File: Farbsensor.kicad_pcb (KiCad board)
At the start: 2 copper layers, 17.8 x 10.5 mm, 9 parts, among them J1 Conn_02x03_Odd_Even, Q1 BCW32

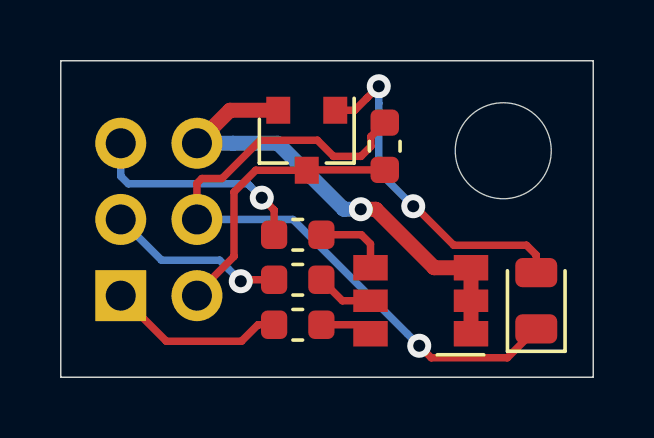
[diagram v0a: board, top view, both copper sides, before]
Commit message: changed pin header assignment, moved resistor
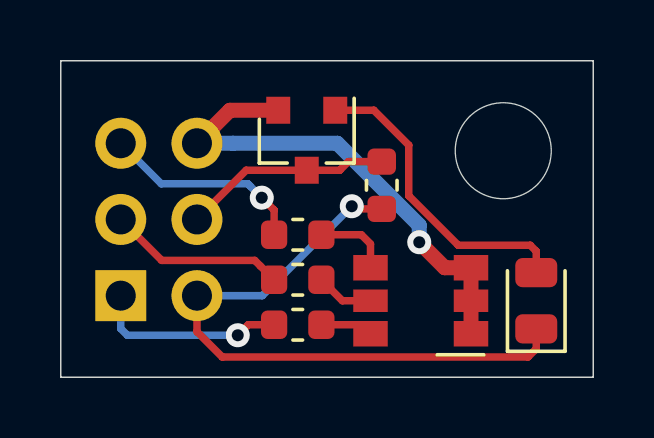
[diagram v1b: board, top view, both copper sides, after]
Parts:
- moved R1 1.30 mm to (107.7, 90.9), turned to 90 degrees
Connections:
- J1 pad 2: /SEN -> +5V
- J1 pad 4: +5V -> /SEN
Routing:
- net /SEN: track 9.30 -> 6.98 mm
- net +5V: track 22.6 -> 21.1 mm
- net Net-(D1-Pad2): track 11.6 -> 10.3 mm, vias 2 -> 0
- net /LED_B: track 7.50 -> 6.86 mm
- net /LED_R: track 5.97 -> 6.45 mm, vias 0 -> 1
- net /LED_G: track 5.99 -> 5.95 mm, vias 1 -> 0

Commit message: Layout überarbeitet, Beschriftungsfehler behoben
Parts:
- moved R2 3.00 mm to (104.9, 95.5)
- moved R4 3.00 mm to (104.9, 92.5)
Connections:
- net Net-(D2-Pad4) renamed /R
- net Net-(D2-Pad5) renamed /G
- net Net-(D2-Pad6) renamed /B
- J1 pad 1: /LED_R -> /LED_B
- J1 pad 5: /LED_B -> /LED_R
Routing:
- net /R: track 1.76 -> 2.56 mm
- net /B: track 2.56 -> 1.76 mm
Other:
- board text added: "Carlo v1.1 Brokering"
- board text removed: "v1.0 Carlo Brokering"

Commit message: Beschriftung geändert
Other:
- board text added: "Farbsensor v1.1"
- board text removed: "Carlo v1.1 Brokering"
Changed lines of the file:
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@@
   (gr_line (start 113.75 94.75) (end 110.7 94.75) (layer B.SilkS) (width 1))
   (target plus (at 104.9 95.55) (size 5) (width 0.05) (layer Edge.Cuts))
-  (gr_text "Carlo v1.1 \nBrokering" (at 108.05 88.15 90) (layer B.SilkS)
-    (effects (font (size 1 1) (thickness 0.2)) (justify left mirror))
+  (gr_text "Farbsensor\nv1.1" (at 108.05 92.05 90) (layer B.SilkS)
+    (effects (font (size 1 1) (thickness 0.2)) (justify mirror))
   )
   (gr_text SEN (at 105.35 92.04 90) (layer B.SilkS)
@@
   (segment (start 102.742081 89.5) (end 101.54 89.5) (width 0.5) (layer B.Cu) (net 3))
   (segment (start 108.95 92.8) (end 108.95 92.234315) (width 0.5) (layer B.Cu) (net 3))
-  (segment (start 107.025 95.55) (end 107.325 95.85) (width 0.25) (layer F.Cu) (net 10))
-  (segment (start 105.6875 95.55) (end 107.025 95.55) (width 0.25) (layer F.Cu) (net 10))
-  (segment (start 106.3875 94.75) (end 107.325 94.75) (width 0.25) (layer F.Cu) (net 9))
-  (segment (start 105.6875 94.05) (end 106.3875 94.75) (width 0.25) (layer F.Cu) (net 9))
-  (segment (start 107.325 92.85625) (end 107.325 93.65) (width 0.25) (layer F.Cu) (net 8))
-  (segment (start 107.01875 92.55) (end 107.325 92.85625) (width 0.25) (layer F.Cu) (net 8))
-  (segment (start 105.6875 92.55) (end 107.01875 92.55) (width 0.25) (layer F.Cu) (net 8))
+  (via (at 102.9 95.9) (size 0.8) (drill 0.4) (layers F.Cu B.Cu) (net 4))
+  (segment (start 104.1125 95.55) (end 103.25 95.55) (width 0.25) (layer F.Cu) (net 4))
+  (segment (start 103.25 95.55) (end 102.9 95.9) (width 0.25) (layer F.Cu) (net 4))
+  (segment (start 99.22 95.9) (end 99 95.68) (width 0.25) (layer B.Cu) (net 4))
+  (segment (start 99 95.68) (end 99 94.58) (width 0.25) (layer B.Cu) (net 4))
+  (segment (start 102.9 95.9) (end 99.22 95.9) (width 0.25) (layer B.Cu) (net 4))
+  (segment (start 103.650888 93.588388) (end 104.1125 94.05) (width 0.25) (layer F.Cu) (net 5))
+  (segment (start 103.467499 93.404999) (end 103.650888 93.588388) (width 0.25) (layer F.Cu) (net 5))
+  (segment (start 100.364999 93.404999) (end 103.467499 93.404999) (width 0.25) (layer F.Cu) (net 5))
+  (segment (start 99 92.04) (end 100.364999 93.404999) (width 0.25) (layer F.Cu) (net 5))
   (segment (start 99 89.5) (end 100.350001 90.850001) (width 0.25) (layer B.Cu) (net 6))
   (segment (start 100.350001 90.850001) (end 103.235107 90.850001) (width 0.25) (layer B.Cu) (net 6))
@@
   (segment (start 104.100095 91.714989) (end 103.700096 91.31499) (width 0.25) (layer F.Cu) (net 6))
   (segment (start 103.300097 90.914991) (end 103.700096 91.31499) (width 0.25) (layer B.Cu) (net 6))
-  (segment (start 103.650888 93.588388) (end 104.1125 94.05) (width 0.25) (layer F.Cu) (net 5))
-  (segment (start 103.467499 93.404999) (end 103.650888 93.588388) (width 0.25) (layer F.Cu) (net 5))
-  (segment (start 100.364999 93.404999) (end 103.467499 93.404999) (width 0.25) (layer F.Cu) (net 5))
-  (segment (start 99 92.04) (end 100.364999 93.404999) (width 0.25) (layer F.Cu) (net 5))
-  (via (at 102.9 95.9) (size 0.8) (drill 0.4) (layers F.Cu B.Cu) (net 4))
-  (segment (start 104.1125 95.55) (end 103.25 95.55) (width 0.25) (layer F.Cu) (net 4))
-  (segment (start 103.25 95.55) (end 102.9 95.9) (width 0.25) (layer F.Cu) (net 4))
-  (segment (start 99.22 95.9) (end 99 95.68) (width 0.25) (layer B.Cu) (net 4))
-  (segment (start 99 95.68) (end 99 94.58) (width 0.25) (layer B.Cu) (net 4))
-  (segment (start 102.9 95.9) (end 99.22 95.9) (width 0.25) (layer B.Cu) (net 4))
   (segment (start 105.2125 90.3875) (end 105.2 90.4) (width 0.25) (layer F.Cu) (net 7))
   (segment (start 105.2 90.4) (end 106.3 90.4) (width 0.25) (layer F.Cu) (net 7))
@@
   (segment (start 101.54 92.04) (end 103.18 90.4) (width 0.25) (layer F.Cu) (net 7))
   (segment (start 106.5875 90.1125) (end 107.7 90.1125) (width 0.25) (layer F.Cu) (net 7))
+  (segment (start 107.325 92.85625) (end 107.325 93.65) (width 0.25) (layer F.Cu) (net 8))
+  (segment (start 107.01875 92.55) (end 107.325 92.85625) (width 0.25) (layer F.Cu) (net 8))
+  (segment (start 105.6875 92.55) (end 107.01875 92.55) (width 0.25) (layer F.Cu) (net 8))
+  (segment (start 106.3875 94.75) (end 107.325 94.75) (width 0.25) (layer F.Cu) (net 9))
+  (segment (start 105.6875 94.05) (end 106.3875 94.75) (width 0.25) (layer F.Cu) (net 9))
+  (segment (start 107.025 95.55) (end 107.325 95.85) (width 0.25) (layer F.Cu) (net 10))
+  (segment (start 105.6875 95.55) (end 107.025 95.55) (width 0.25) (layer F.Cu) (net 10))
 )
